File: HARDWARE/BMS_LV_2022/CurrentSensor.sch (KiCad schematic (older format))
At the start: 3 parts

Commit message: Hardware update; -changes after team review;
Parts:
- C?: value 1n -> 1nF
- C?: value 1u -> 1uF
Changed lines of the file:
@@
 AR Path="/62C2DD72/62C4104D" Ref="C?"  Part="1"
 F 0 "C?" H 3192 2096 50  0000 L CNN
-F 1 "1n" H 3192 2005 50  0000 L CNN
+F 1 "1nF" H 3192 2005 50  0000 L CNN
 F 2 "" H 3100 2050 50  0001 C CNN
 F 3 "~" H 3100 2050 50  0001 C CNN
@@
 AR Path="/62C2DD72/62C4105A" Ref="C?"  Part="1"
 F 0 "C?" H 3842 1846 50  0000 L CNN
-F 1 "1u" H 3842 1755 50  0000 L CNN
+F 1 "1uF" H 3842 1755 50  0000 L CNN
 F 2 "" H 3750 1800 50  0001 C CNN
 F 3 "~" H 3750 1800 50  0001 C CNN

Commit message: Electrical Rules Checker fixes
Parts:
- gave numbers to parts that had none: 3
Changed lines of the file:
@@
 P 2600 1800
 AR Path="/62C41044" Ref="U?"  Part="1"
-AR Path="/62C2DD72/62C41044" Ref="U?"  Part="1"
-F 0 "U?" H 2600 2381 50  0000 C CNN
+AR Path="/62C2DD72/62C41044" Ref="U5"  Part="1"
+F 0 "U5" H 2600 2381 50  0000 C CNN
 F 1 "ACHS-7123" H 2600 2290 50  0000 C CNN
 F 2 "Package_SO:SOIC-8_3.9x4.9mm_P1.27mm" H 2700 1450 50  0001 L CIN
@@
 P 3100 2050
 AR Path="/62C4104D" Ref="C?"  Part="1"
-AR Path="/62C2DD72/62C4104D" Ref="C?"  Part="1"
-F 0 "C?" H 3192 2096 50  0000 L CNN
+AR Path="/62C2DD72/62C4104D" Ref="C42"  Part="1"
+F 0 "C42" H 3192 2096 50  0000 L CNN
 F 1 "1nF" H 3192 2005 50  0000 L CNN
 F 2 "" H 3100 2050 50  0001 C CNN
@@
 P 3750 1800
 AR Path="/62C4105A" Ref="C?"  Part="1"
-AR Path="/62C2DD72/62C4105A" Ref="C?"  Part="1"
-F 0 "C?" H 3842 1846 50  0000 L CNN
+AR Path="/62C2DD72/62C4105A" Ref="C43"  Part="1"
+F 0 "C43" H 3842 1846 50  0000 L CNN
 F 1 "1uF" H 3842 1755 50  0000 L CNN
 F 2 "" H 3750 1800 50  0001 C CNN
@@
 P 3750 2300
 AR Path="/62C41064" Ref="#PWR?"  Part="1"
-AR Path="/62C2DD72/62C41064" Ref="#PWR?"  Part="1"
-F 0 "#PWR?" H 3750 2050 50  0001 C CNN
+AR Path="/62C2DD72/62C41064" Ref="#PWR050"  Part="1"
+F 0 "#PWR050" H 3750 2050 50  0001 C CNN
 F 1 "GND" H 3755 2127 50  0000 C CNN
 F 2 "" H 3750 2300 50  0001 C CNN
@@
 P 3750 1350
 AR Path="/62C4106C" Ref="#PWR?"  Part="1"
-AR Path="/62C2DD72/62C4106C" Ref="#PWR?"  Part="1"
-F 0 "#PWR?" H 3750 1200 50  0001 C CNN
+AR Path="/62C2DD72/62C4106C" Ref="#PWR049"  Part="1"
+F 0 "#PWR049" H 3750 1200 50  0001 C CNN
 F 1 "+5V" H 3765 1523 50  0000 C CNN
 F 2 "" H 3750 1350 50  0001 C CNN

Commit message: Most of the footprints added
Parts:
- C42, C43: footprint (none) -> Capacitor_SMD:C_0603_1608Metric
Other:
- moved on the sheet: C42, C43, U5
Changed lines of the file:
@@
 EELAYER 30 0
 EELAYER END
-$Descr User 5906 4725
+$Descr A4 11693 8268
 encoding utf-8
 Sheet 13 13
@@
 L Sensor_Current:ACS712xLCTR-30A U?
 U 1 1 62C41044
-P 2600 1800
+P 5400 3700
 AR Path="/62C41044" Ref="U?"  Part="1"
 AR Path="/62C2DD72/62C41044" Ref="U5"  Part="1"
-F 0 "U5" H 2600 2381 50  0000 C CNN
-F 1 "ACHS-7123" H 2600 2290 50  0000 C CNN
-F 2 "Package_SO:SOIC-8_3.9x4.9mm_P1.27mm" H 2700 1450 50  0001 L CIN
-F 3 "https://download.kamami.pl/p586603-ACHS-712x-DS101_2018-02-28.pdf" H 2600 1800 50  0001 C CNN
-	1    2600 1800
+F 0 "U5" H 5400 4281 50  0000 C CNN
+F 1 "ACHS-7123" H 5400 4190 50  0000 C CNN
+F 2 "Package_SO:SOIC-8_3.9x4.9mm_P1.27mm" H 5500 3350 50  0001 L CIN
+F 3 "https://download.kamami.pl/p586603-ACHS-712x-DS101_2018-02-28.pdf" H 5400 3700 50  0001 C CNN
+	1    5400 3700
 	1    0    0    -1
 $EndComp
 Wire Wire Line
-	2200 1600 2050 1600
+	5000 3500 4850 3500
 Wire Wire Line
-	2200 2000 2050 2000
+	5000 3900 4850 3900
 Wire Wire Line
-	2600 2200 2600 2250
+	5400 4100 5400 4150
 $Comp
 L Device:C_Small C?
 U 1 1 62C4104D
-P 3100 2050
+P 5900 3950
 AR Path="/62C4104D" Ref="C?"  Part="1"
 AR Path="/62C2DD72/62C4104D" Ref="C42"  Part="1"
-F 0 "C42" H 3192 2096 50  0000 L CNN
-F 1 "1nF" H 3192 2005 50  0000 L CNN
-F 2 "" H 3100 2050 50  0001 C CNN
-F 3 "~" H 3100 2050 50  0001 C CNN
-	1    3100 2050
+F 0 "C42" H 5992 3996 50  0000 L CNN
+F 1 "1nF" H 5992 3905 50  0000 L CNN
+F 2 "Capacitor_SMD:C_0603_1608Metric" H 5900 3950 50  0001 C CNN
+F 3 "~" H 5900 3950 50  0001 C CNN
+	1    5900 3950
 	1    0    0    -1
 $EndComp
 Wire Wire Line
-	3000 1900 3100 1900
+	5800 3800 5900 3800
 Wire Wire Line
-	3100 1900 3100 1950
+	5900 3800 5900 3850
 Wire Wire Line
-	3100 2150 3100 2250
+	5900 4050 5900 4150
 Wire Wire Line
-	2600 2250 3100 2250
+	5400 4150 5900 4150
 Wire Wire Line
-	3000 1800 3050 1800
+	5800 3700 5850 3700
 $Comp
 L Device:C_Small C?
 U 1 1 62C4105A
-P 3750 1800
+P 6550 3700
 AR Path="/62C4105A" Ref="C?"  Part="1"
 AR Path="/62C2DD72/62C4105A" Ref="C43"  Part="1"
-F 0 "C43" H 3842 1846 50  0000 L CNN
-F 1 "1uF" H 3842 1755 50  0000 L CNN
-F 2 "" H 3750 1800 50  0001 C CNN
-F 3 "~" H 3750 1800 50  0001 C CNN
-	1    3750 1800
+F 0 "C43" H 6642 3746 50  0000 L CNN
+F 1 "1uF" H 6642 3655 50  0000 L CNN
+F 2 "Capacitor_SMD:C_0603_1608Metric" H 6550 3700 50  0001 C CNN
+F 3 "~" H 6550 3700 50  0001 C CNN
+	1    6550 3700
 	1    0    0    -1
 $EndComp
 Wire Wire Line
-	3750 2250 3750 1900
+	6550 4150 6550 3800
 Wire Wire Line
-	3750 1700 3750 1400
+	6550 3600 6550 3300
 $Comp
 L power:GND #PWR?
 U 1 1 62C41064
-P 3750 2300
+P 6550 4200
 AR Path="/62C41064" Ref="#PWR?"  Part="1"
 AR Path="/62C2DD72/62C41064" Ref="#PWR050"  Part="1"
-F 0 "#PWR050" H 3750 2050 50  0001 C CNN
-F 1 "GND" H 3755 2127 50  0000 C CNN
-F 2 "" H 3750 2300 50  0001 C CNN
-F 3 "" H 3750 2300 50  0001 C CNN
-	1    3750 2300
+F 0 "#PWR050" H 6550 3950 50  0001 C CNN
+F 1 "GND" H 6555 4027 50  0000 C CNN
+F 2 "" H 6550 4200 50  0001 C CNN
+F 3 "" H 6550 4200 50  0001 C CNN
+	1    6550 4200
 	1    0    0    -1
 $EndComp
 Wire Wire Line
-	3750 2250 3750 2300
-Connection ~ 3750 2250
+	6550 4150 6550 4200
+Connection ~ 6550 4150
 $Comp
 L power:+5V #PWR?
 U 1 1 62C4106C
-P 3750 1350
+P 6550 3250
 AR Path="/62C4106C" Ref="#PWR?"  Part="1"
 AR Path="/62C2DD72/62C4106C" Ref="#PWR049"  Part="1"
-F 0 "#PWR049" H 3750 1200 50  0001 C CNN
-F 1 "+5V" H 3765 1523 50  0000 C CNN
-F 2 "" H 3750 1350 50  0001 C CNN
-F 3 "" H 3750 1350 50  0001 C CNN
-	1    3750 1350
+F 0 "#PWR049" H 6550 3100 50  0001 C CNN
+F 1 "+5V" H 6565 3423 50  0000 C CNN
+F 2 "" H 6550 3250 50  0001 C CNN
+F 3 "" H 6550 3250 50  0001 C CNN
+	1    6550 3250
 	1    0    0    -1
 $EndComp
 Wire Wire Line
-	3750 1350 3750 1400
-Connection ~ 3750 1400
-Text HLabel 2050 1600 0    50   Input ~ 0
+	6550 3250 6550 3300
+Connection ~ 6550 3300
+Text HLabel 4850 3500 0    50   Input ~ 0
 CS_IP+
-Text HLabel 2050 2000 0    50   Output ~ 0
+Text HLabel 4850 3900 0    50   Output ~ 0
 V_Out
-Text HLabel 3050 1800 2    50   Output ~ 0
+Text HLabel 5850 3700 2    50   Output ~ 0
 CurrentSensor
 Wire Wire Line
-	3100 2250 3750 2250
-Connection ~ 3100 2250
+	5900 4150 6550 4150
+Connection ~ 5900 4150
 Wire Wire Line
-	2600 1400 3750 1400
+	5400 3300 6550 3300
 $EndSCHEMATC

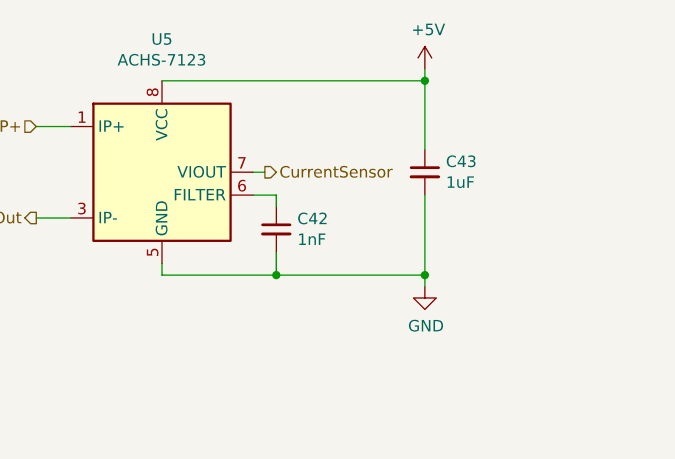
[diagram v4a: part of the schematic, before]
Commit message: Voltage divider in current sensor section added
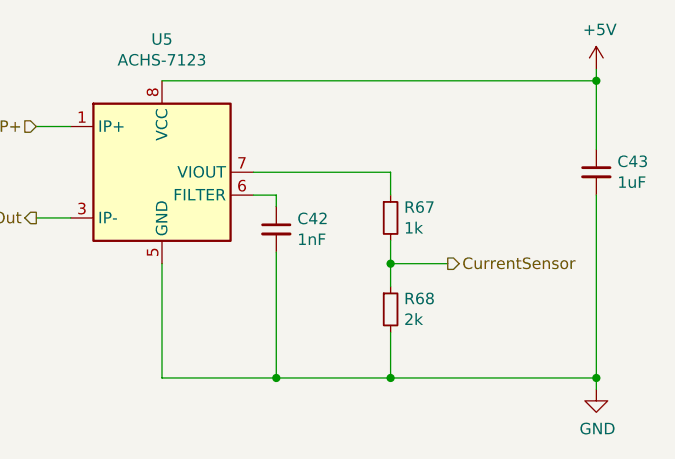
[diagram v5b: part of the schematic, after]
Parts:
- added R67: 1k, Resistor_SMD:R_0603_1608Metric, symbol Device:R_Small
- added R68: 2k, Resistor_SMD:R_0603_1608Metric, symbol Device:R_Small
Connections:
- net CurrentSensor: now also R67.2, R68.1; no longer U5.7 (VIOUT)
- net GND: now also R68.2
- new net: R67.1, U5.7 (VIOUT)
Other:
- moved on the sheet: C43
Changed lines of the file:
@@
 Wire Wire Line
 	5000 3900 4850 3900
-Wire Wire Line
-	5400 4100 5400 4150
 $Comp
 L Device:C_Small C?
@@
 	5900 3800 5900 3850
 Wire Wire Line
-	5900 4050 5900 4150
-Wire Wire Line
-	5400 4150 5900 4150
-Wire Wire Line
-	5800 3700 5850 3700
+	5400 4600 5900 4600
 $Comp
 L Device:C_Small C?
 U 1 1 62C4105A
-P 6550 3700
+P 7300 3700
 AR Path="/62C4105A" Ref="C?"  Part="1"
 AR Path="/62C2DD72/62C4105A" Ref="C43"  Part="1"
-F 0 "C43" H 6642 3746 50  0000 L CNN
-F 1 "1uF" H 6642 3655 50  0000 L CNN
-F 2 "Capacitor_SMD:C_0603_1608Metric" H 6550 3700 50  0001 C CNN
-F 3 "~" H 6550 3700 50  0001 C CNN
-	1    6550 3700
+F 0 "C43" H 7392 3746 50  0000 L CNN
+F 1 "1uF" H 7392 3655 50  0000 L CNN
+F 2 "Capacitor_SMD:C_0603_1608Metric" H 7300 3700 50  0001 C CNN
+F 3 "~" H 7300 3700 50  0001 C CNN
+	1    7300 3700
 	1    0    0    -1
 $EndComp
 Wire Wire Line
-	6550 4150 6550 3800
-Wire Wire Line
-	6550 3600 6550 3300
+	7300 3600 7300 3300
 $Comp
 L power:GND #PWR?
 U 1 1 62C41064
-P 6550 4200
+P 7300 4650
 AR Path="/62C41064" Ref="#PWR?"  Part="1"
 AR Path="/62C2DD72/62C41064" Ref="#PWR050"  Part="1"
-F 0 "#PWR050" H 6550 3950 50  0001 C CNN
-F 1 "GND" H 6555 4027 50  0000 C CNN
-F 2 "" H 6550 4200 50  0001 C CNN
-F 3 "" H 6550 4200 50  0001 C CNN
-	1    6550 4200
+F 0 "#PWR050" H 7300 4400 50  0001 C CNN
+F 1 "GND" H 7305 4477 50  0000 C CNN
+F 2 "" H 7300 4650 50  0001 C CNN
+F 3 "" H 7300 4650 50  0001 C CNN
+	1    7300 4650
 	1    0    0    -1
 $EndComp
 Wire Wire Line
-	6550 4150 6550 4200
-Connection ~ 6550 4150
+	7300 4600 7300 4650
+Connection ~ 7300 4600
 $Comp
 L power:+5V #PWR?
 U 1 1 62C4106C
-P 6550 3250
+P 7300 3250
 AR Path="/62C4106C" Ref="#PWR?"  Part="1"
 AR Path="/62C2DD72/62C4106C" Ref="#PWR049"  Part="1"
-F 0 "#PWR049" H 6550 3100 50  0001 C CNN
-F 1 "+5V" H 6565 3423 50  0000 C CNN
-F 2 "" H 6550 3250 50  0001 C CNN
-F 3 "" H 6550 3250 50  0001 C CNN
-	1    6550 3250
+F 0 "#PWR049" H 7300 3100 50  0001 C CNN
+F 1 "+5V" H 7315 3423 50  0000 C CNN
+F 2 "" H 7300 3250 50  0001 C CNN
+F 3 "" H 7300 3250 50  0001 C CNN
+	1    7300 3250
 	1    0    0    -1
 $EndComp
 Wire Wire Line
-	6550 3250 6550 3300
-Connection ~ 6550 3300
+	7300 3250 7300 3300
+Connection ~ 7300 3300
 Text HLabel 4850 3500 0    50   Input ~ 0
 CS_IP+
 Text HLabel 4850 3900 0    50   Output ~ 0
 V_Out
-Text HLabel 5850 3700 2    50   Output ~ 0
+Text HLabel 6650 4100 2    50   Output ~ 0
 CurrentSensor
 Wire Wire Line
-	5900 4150 6550 4150
-Connection ~ 5900 4150
+	5400 4100 5400 4600
 Wire Wire Line
-	5400 3300 6550 3300
+	5900 4050 5900 4600
+Wire Wire Line
+	7300 3800 7300 4600
+Wire Wire Line
+	5900 4600 6400 4600
+Connection ~ 5900 4600
+Wire Wire Line
+	5400 3300 7300 3300
+$Comp
+L Device:R_Small R67
+U 1 1 62BB2CC9
+P 6400 3900
+F 0 "R67" H 6459 3946 50  0000 L CNN
+F 1 "1k" H 6459 3855 50  0000 L CNN
+F 2 "Resistor_SMD:R_0603_1608Metric" H 6400 3900 50  0001 C CNN
+F 3 "~" H 6400 3900 50  0001 C CNN
+	1    6400 3900
+	1    0    0    -1
+$EndComp
+$Comp
+L Device:R_Small R68
+U 1 1 62BB3BF9
+P 6400 4300
+F 0 "R68" H 6459 4346 50  0000 L CNN
+F 1 "2k" H 6459 4255 50  0000 L CNN
+F 2 "Resistor_SMD:R_0603_1608Metric" H 6400 4300 50  0001 C CNN
+F 3 "~" H 6400 4300 50  0001 C CNN
+	1    6400 4300
+	1    0    0    -1
+$EndComp
+Wire Wire Line
+	6400 3700 6400 3800
+Wire Wire Line
+	5800 3700 6400 3700
+Wire Wire Line
+	6400 4000 6400 4100
+Connection ~ 6400 4600
+Wire Wire Line
+	6400 4600 7300 4600
+Wire Wire Line
+	6650 4100 6400 4100
+Wire Wire Line
+	6400 4100 6400 4200
+Connection ~ 6400 4100
+Wire Wire Line
+	6400 4400 6400 4600
 $EndSCHEMATC
